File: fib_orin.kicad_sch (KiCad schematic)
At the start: 1 part, among them J1201 Orin Nano

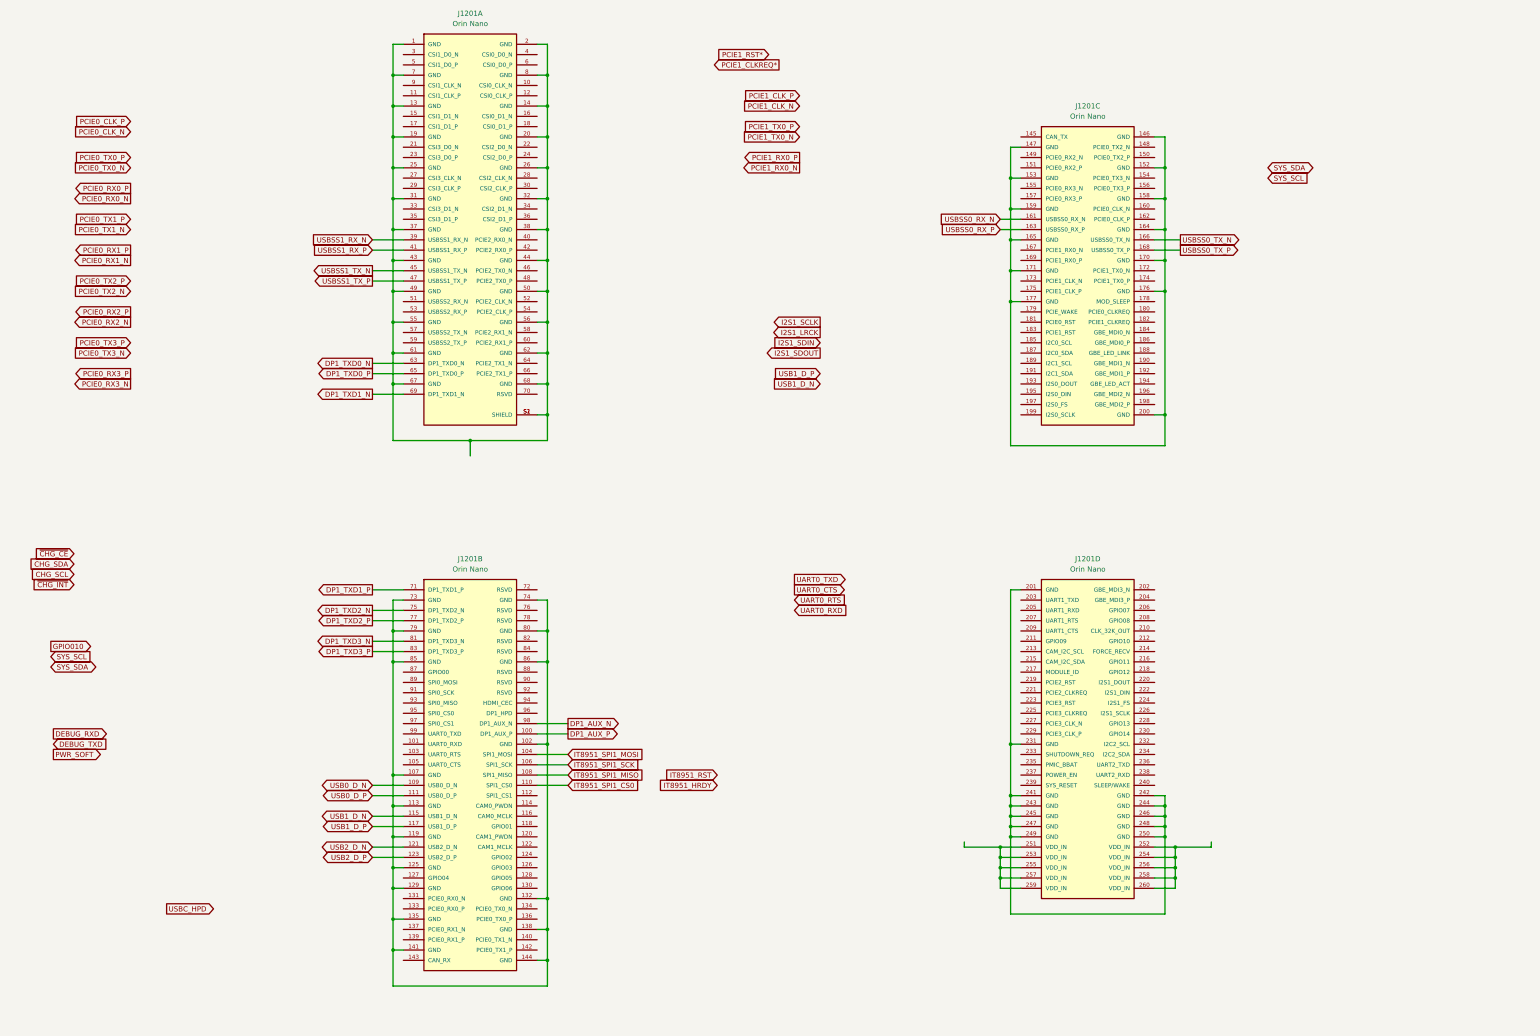
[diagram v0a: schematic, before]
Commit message: continuing schematic work for pcie and other high speed interfaces
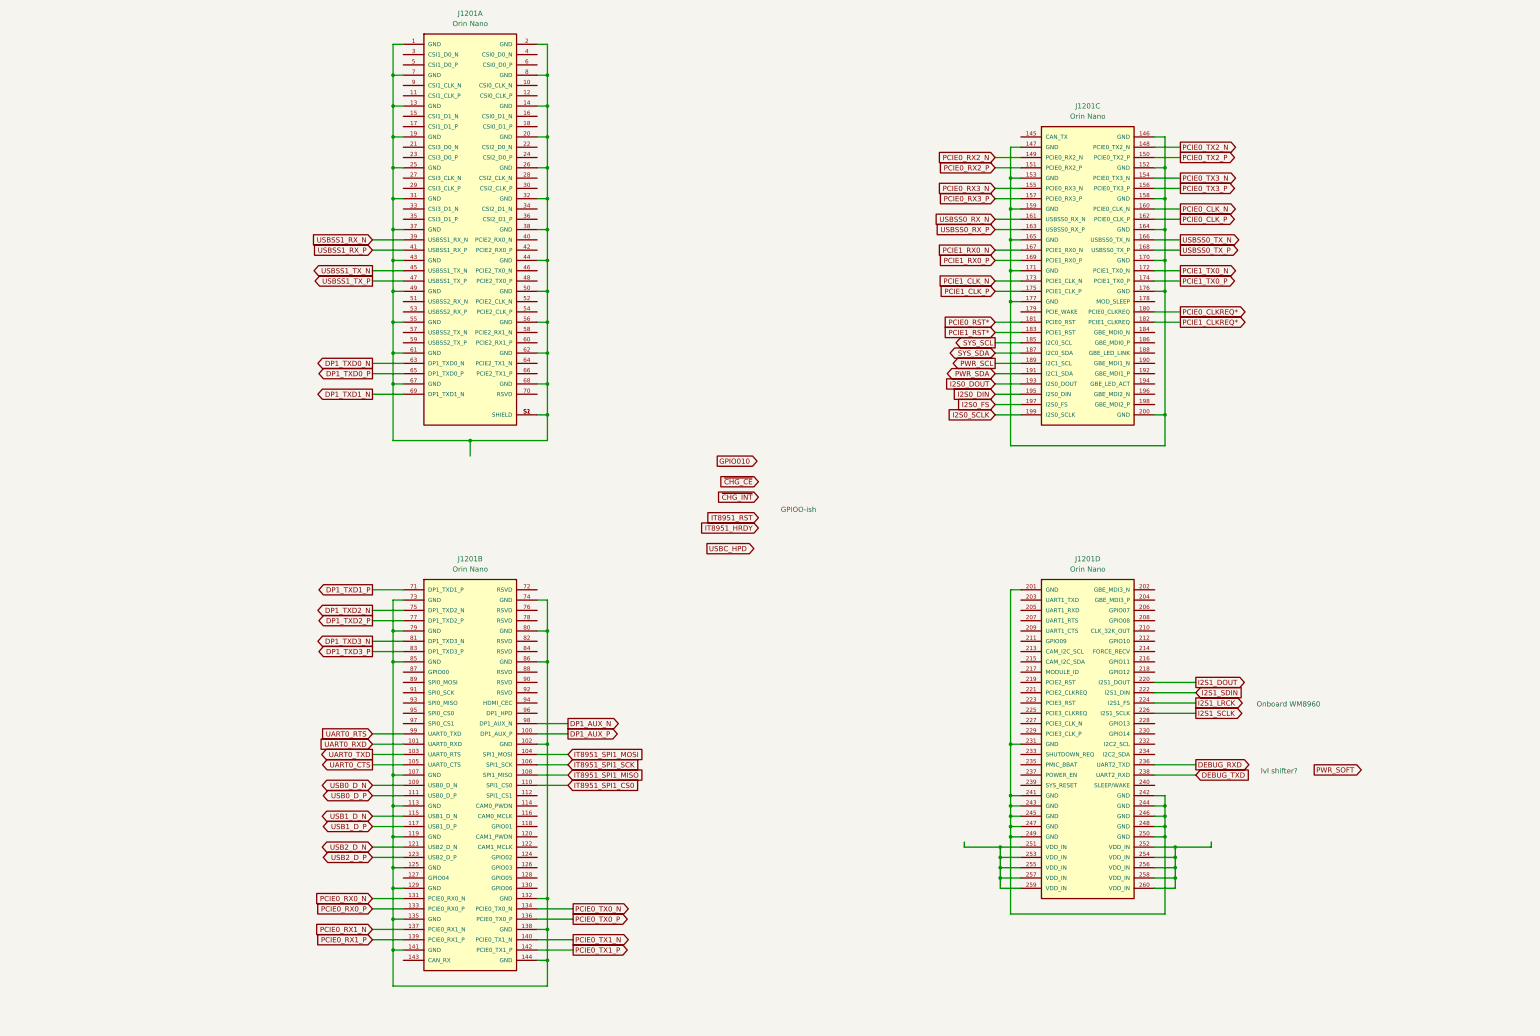
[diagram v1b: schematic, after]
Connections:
- net DEBUG_RXD: now also J1201.236 (UART2_TXD)
- net DEBUG_TXD: now also J1201.238 (UART2_RXD)
- net I2S1_LRCK: now also J1201.224 (I2S1_FS)
- net I2S1_SCLK: now also J1201.226 (I2S1_SCLK)
- net I2S1_SDIN: now also J1201.222 (I2S1_DIN)
- net PCIE0_CLK_N: now also J1201.160 (PCIE0_CLK_N)
- net PCIE0_CLK_P: now also J1201.162 (PCIE0_CLK_P)
- net PCIE0_RX0_N: now also J1201.131 (PCIE0_RX0_N)
- net PCIE0_RX0_P: now also J1201.133 (PCIE0_RX0_P)
- net PCIE0_RX1_N: now also J1201.137 (PCIE0_RX1_N)
- net PCIE0_RX1_P: now also J1201.139 (PCIE0_RX1_P)
- net PCIE0_RX2_N: now also J1201.149 (PCIE0_RX2_N)
- net PCIE0_RX2_P: now also J1201.151 (PCIE0_RX2_P)
- net PCIE0_RX3_N: now also J1201.155 (PCIE0_RX3_N)
- net PCIE0_RX3_P: now also J1201.157 (PCIE0_RX3_P)
- net PCIE0_TX0_N: now also J1201.134 (PCIE0_TX0_N)
- net PCIE0_TX0_P: now also J1201.136 (PCIE0_TX0_P)
- net PCIE0_TX1_N: now also J1201.140 (PCIE0_TX1_N)
- net PCIE0_TX1_P: now also J1201.142 (PCIE0_TX1_P)
- net PCIE0_TX2_N: now also J1201.148 (PCIE0_TX2_N)
- net PCIE0_TX2_P: now also J1201.150 (PCIE0_TX2_P)
- net PCIE0_TX3_N: now also J1201.154 (PCIE0_TX3_N)
- net PCIE0_TX3_P: now also J1201.156 (PCIE0_TX3_P)
- net PCIE1_CLKREQ*: now also J1201.182 (PCIE1_CLKREQ)
- net PCIE1_CLK_N: now also J1201.173 (PCIE1_CLK_N)
- net PCIE1_CLK_P: now also J1201.175 (PCIE1_CLK_P)
- net PCIE1_RST*: now also J1201.183 (PCIE1_RST)
- net PCIE1_RX0_N: now also J1201.167 (PCIE1_RX0_N)
- net PCIE1_RX0_P: now also J1201.169 (PCIE1_RX0_P)
- net PCIE1_TX0_N: now also J1201.172 (PCIE1_TX0_N)
- net PCIE1_TX0_P: now also J1201.174 (PCIE1_TX0_P)
- net SYS_SCL: now also J1201.185 (I2C0_SCL)
- net SYS_SDA: now also J1201.187 (I2C0_SDA)
- net UART0_CTS: now also J1201.105 (UART0_CTS)
- net UART0_RTS: now also J1201.99 (UART0_TXD)
- net UART0_RXD: now also J1201.101 (UART0_RXD)
- net UART0_TXD: now also J1201.103 (UART0_RTS)
- net I2S1_DOUT: now reaches J1201.220 (I2S1_DOUT)
- net PCIE0_CLKREQ*: now reaches J1201.180 (PCIE0_CLKREQ)
- net PCIE0_RST*: now reaches J1201.181 (PCIE0_RST)
- net PWR_SCL: now reaches J1201.189 (I2C1_SCL)
- net PWR_SDA: now reaches J1201.191 (I2C1_SDA)
- net I2S0_DOUT: now reaches J1201.193 (I2S0_DOUT)
- net I2S0_DIN: now reaches J1201.195 (I2S0_DIN)
- net I2S0_FS: now reaches J1201.197 (I2S0_FS)
- net I2S0_SCLK: now reaches J1201.199 (I2S0_SCLK)
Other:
- note added: "GPIOO-ish"
- note added: "Onboard WM8960"
- note added: "lvl shifter?"

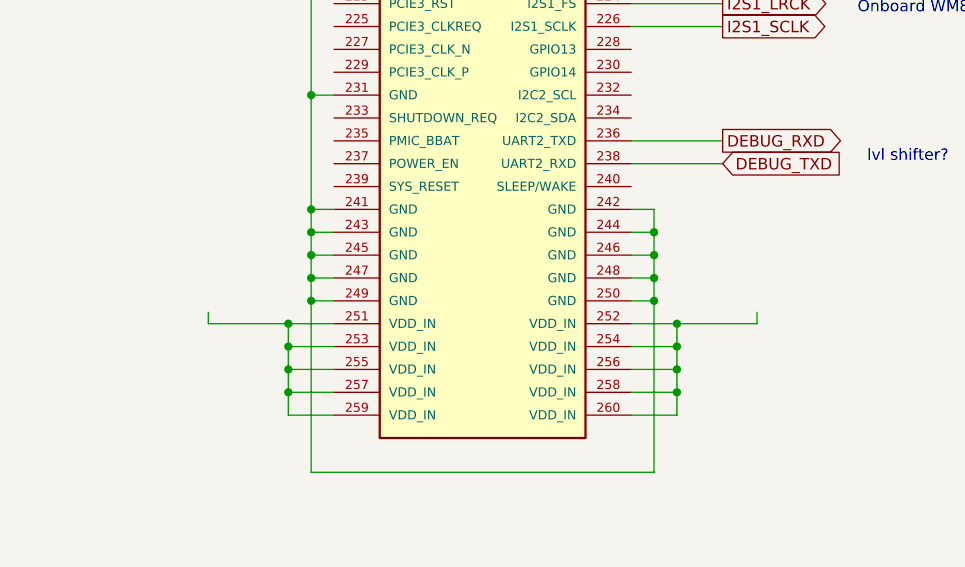
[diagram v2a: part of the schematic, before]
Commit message: added notest regarding the audio codec
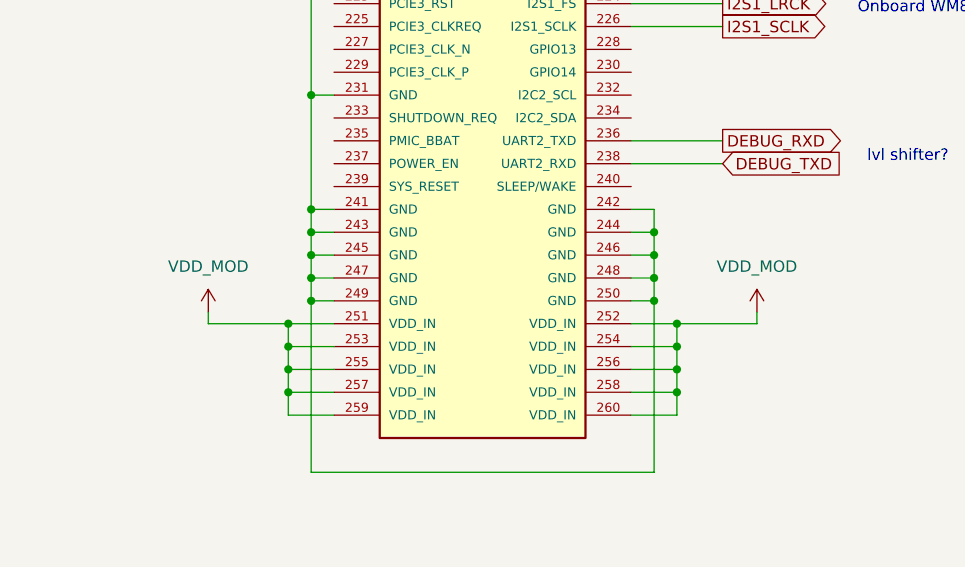
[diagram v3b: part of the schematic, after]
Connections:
- net VDD_MOD: now reaches J1201.251 (VDD_IN), J1201.253 (VDD_IN), J1201.255 (VDD_IN), J1201.257 (VDD_IN), J1201.259 (VDD_IN)
- net VDD_MOD: now also J1201.252 (VDD_IN), J1201.254 (VDD_IN), J1201.256 (VDD_IN), J1201.258 (VDD_IN), J1201.260 (VDD_IN)
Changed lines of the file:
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@@
+	)
+	(symbol
+		(lib_id "power:+5V")
+		(at 254 229.87 0)
+		(unit 1)
+		(exclude_from_sim no)
+		(in_bom yes)
+		(on_board yes)
+		(dnp no)
+		(fields_autoplaced yes)
+		(property "Reference" "#PWR01"
+			(at 254 233.68 0)
+			(effects
+				(font
+					(size 1.27 1.27)
+				)
+				(hide yes)
+			)
+		)
+		(property "Value" "VDD_MOD"
+			(at 254 224.79 0)
+			(effects
+				(font
+					(size 1.27 1.27)
+				)
+			)
+		)
+		(property "Footprint" ""
+			(at 254 229.87 0)
+			(effects
+				(font
+					(size 1.27 1.27)
+				)
+				(hide yes)
+			)
+		)
+		(property "Datasheet" ""
+			(at 254 229.87 0)
+			(effects
+				(font
+					(size 1.27 1.27)
+				)
+				(hide yes)
+			)
+		)
+		(property "Description" "Power symbol creates a global label with name \"+5V\""
+			(at 254 229.87 0)
+			(effects
+				(font
+					(size 1.27 1.27)
+				)
+				(hide yes)
+			)
+		)
+		(pin "1"
+		)
+		(instances
+			(project "Fibel2"
+				(path "/862c21e2-7ec9-4f80-a33c-aad02ea9423e/36a293ae-b0d7-4698-aa86-662a0ac946ae"
+					(reference "#PWR01")
+					(unit 1)
+				)
+			)
+		)
+	)
+	(symbol
+		(lib_id "power:+5V")
+		(at 314.96 229.87 0)
+		(unit 1)
+		(exclude_from_sim no)
+		(in_bom yes)
+		(on_board yes)
+		(dnp no)
+		(fields_autoplaced yes)
+		(property "Reference" "#PWR02"
+			(at 314.96 233.68 0)
+			(effects
+				(font
+					(size 1.27 1.27)
+				)
+				(hide yes)
+			)
+		)
+		(property "Value" "VDD_MOD"
+			(at 314.96 224.79 0)
+			(effects
+				(font
+					(size 1.27 1.27)
+				)
+			)
+		)
+		(property "Footprint" ""
+			(at 314.96 229.87 0)
+			(effects
+				(font
+					(size 1.27 1.27)
+				)
+				(hide yes)
+			)
+		)
+		(property "Datasheet" ""
+			(at 314.96 229.87 0)
+			(effects
+				(font
+					(size 1.27 1.27)
+				)
+				(hide yes)
+			)
+		)
+		(property "Description" "Power symbol creates a global label with name \"+5V\""
+			(at 314.96 229.87 0)
+			(effects
+				(font
+					(size 1.27 1.27)
+				)
+				(hide yes)
+			)
+		)
+		(pin "1"
+		)
+		(instances
+			(project "Fibel2"
+				(path "/862c21e2-7ec9-4f80-a33c-aad02ea9423e/36a293ae-b0d7-4698-aa86-662a0ac946ae"
+					(reference "#PWR02")
+					(unit 1)
+				)
+			)
+		)
 	)
 	(symbol

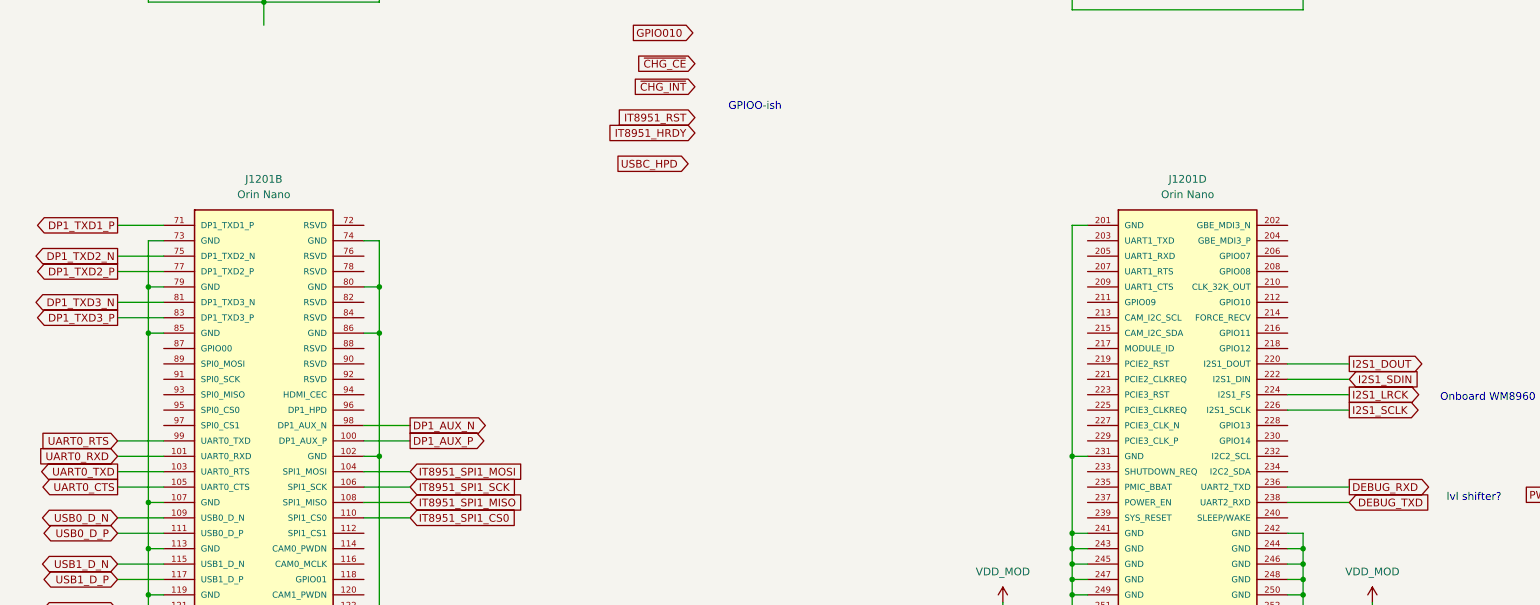
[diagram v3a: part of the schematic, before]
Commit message: added buck converter, refactoored peripherals and updated gpio/SPI/i2c mapping
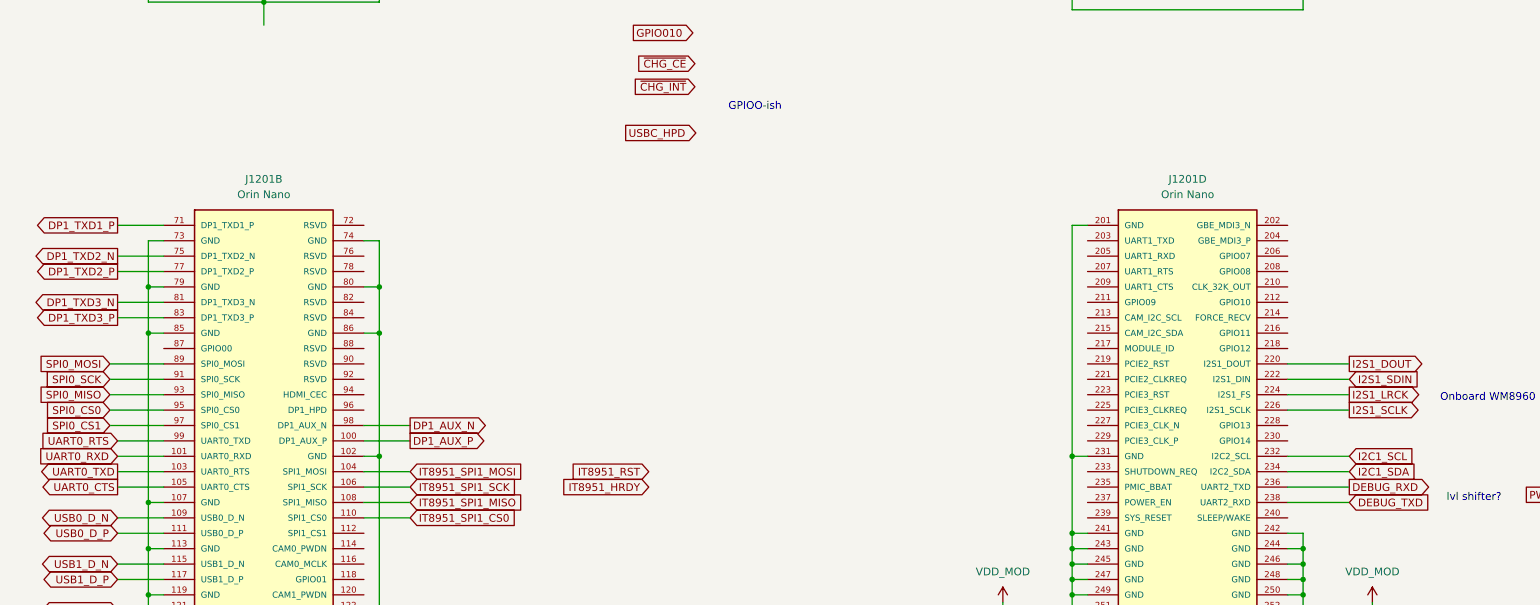
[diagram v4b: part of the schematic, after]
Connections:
- net SPI0_MOSI: now reaches J1201.89 (SPI0_MOSI)
- net SPI0_SCK: now reaches J1201.91 (SPI0_SCK)
- net SPI0_MISO: now reaches J1201.93 (SPI0_MISO)
- net SPI0_CS0: now reaches J1201.95 (SPI0_CS0)
- net SPI0_CS1: now reaches J1201.97 (SPI0_CS1)
- net I2C1_SCL: now reaches J1201.232 (I2C2_SCL)
- net I2C1_SDA: now reaches J1201.234 (I2C2_SDA)
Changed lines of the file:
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@@
 	(wire
 		(pts
+			(xy 106.68 195.58) (xy 115.57 195.58)
+		)
+		(stroke
+			(width 0)
+			(type default)
+		)
+	)
+	(wire
+		(pts
 			(xy 261.62 121.92) (xy 267.97 121.92)
 		)
@@
 	(wire
 		(pts
+			(xy 106.68 190.5) (xy 115.57 190.5)
+		)
+		(stroke
+			(width 0)
+			(type default)
+		)
+	)
+	(wire
+		(pts
 			(xy 311.15 195.58) (xy 300.99 195.58)
 		)
@@
 	(wire
 		(pts
+			(xy 311.15 208.28) (xy 300.99 208.28)
+		)
+		(stroke
+			(width 0)
+			(type default)
+		)
+	)
+	(wire
+		(pts
 			(xy 107.95 251.46) (xy 115.57 251.46)
 		)
@@
 	(wire
 		(pts
+			(xy 106.68 193.04) (xy 115.57 193.04)
+		)
+		(stroke
+			(width 0)
+			(type default)
+		)
+	)
+	(wire
+		(pts
 			(xy 303.53 223.52) (xy 303.53 220.98)
 		)
@@
 	(wire
 		(pts
+			(xy 311.15 205.74) (xy 300.99 205.74)
+		)
+		(stroke
+			(width 0)
+			(type default)
+		)
+	)
+	(wire
+		(pts
 			(xy 113.03 177.8) (xy 115.57 177.8)
 		)
@@
 	(wire
 		(pts
+			(xy 106.68 200.66) (xy 115.57 200.66)
+		)
+		(stroke
+			(width 0)
+			(type default)
+		)
+	)
+	(wire
+		(pts
 			(xy 113.03 55.88) (xy 113.03 63.5)
 		)
@@
 	(wire
 		(pts
+			(xy 106.68 198.12) (xy 115.57 198.12)
+		)
+		(stroke
+			(width 0)
+			(type default)
+		)
+	)
+	(wire
+		(pts
 			(xy 113.03 71.12) (xy 113.03 78.74)
 		)
@@
 		)
 	)
+	(global_label "I2C1_SDA"
+		(shape input)
+		(at 311.15 208.28 0)
+		(fields_autoplaced yes)
+		(effects
+			(font
+				(size 1.27 1.27)
+			)
+			(justify left)
+		)
+		(property "Intersheetrefs" "${INTERSHEET_REFS}"
+			(at 322.9647 208.28 0)
+			(effects
+				(font
+					(size 1.27 1.27)
+				)
+				(justify left)
+				(hide yes)
+			)
+		)
+	)
 	(global_label "USB2_D_P"
 		(shape bidirectional)
@@
 	(global_label "IT8951_RST"
 		(shape input)
-		(at 203.2 149.86 180)
+		(at 195.58 208.28 180)
+		(fields_autoplaced yes)
+		(effects
+			(font
+				(size 1.27 1.27)
+			)
+			(justify right)
+		)
+		(property "Intersheetrefs" "${INTERSHEET_REFS}"
+			(at 181.7697 208.28 0)
+			(effects
+				(font
+					(size 1.27 1.27)
+				)
+				(justify right)
+				(hide yes)
+			)
+		)
+	)
+	(global_label "SPI0_MISO"
+		(shape input)
+		(at 106.68 195.58 180)
 		(fields_autoplaced yes)
 		(effects
@@
 		)
 		(property "Intersheetrefs" "${INTERSHEET_REFS}"
-			(at 189.3897 149.86 0)
+			(at 93.8372 195.58 0)
 			(effects
 				(font
@@
 		)
 	)
+	(global_label "SPI0_SCK"
+		(shape input)
+		(at 106.68 193.04 180)
+		(fields_autoplaced yes)
+		(effects
+			(font
+				(size 1.27 1.27)
+			)
+			(justify right)
+		)
+		(property "Intersheetrefs" "${INTERSHEET_REFS}"
+			(at 94.6839 193.04 0)
+			(effects
+				(font
+					(size 1.27 1.27)
+				)
+				(justify right)
+				(hide yes)
+			)
+		)
+	)
 	(global_label "USBSS0_RX_N"
 		(shape input)
@@
 		)
 	)
+	(global_label "SPI0_CS0"
+		(shape input)
+		(at 106.68 198.12 180)
+		(fields_autoplaced yes)
+		(effects
+			(font
+				(size 1.27 1.27)
+			)
+			(justify right)
+		)
+		(property "Intersheetrefs" "${INTERSHEET_REFS}"
+			(at 94.7444 198.12 0)
+			(effects
+				(font
+					(size 1.27 1.27)
+				)
+				(justify right)
+				(hide yes)
+			)
+		)
+	)
 	(global_label "PCIE0_RST*"
 		(shape input)
@@
 		)
 	)
+	(global_label "SPI0_MOSI"
+		(shape input)
+		(at 106.68 190.5 180)
+		(fields_autoplaced yes)
+		(effects
+			(font
+				(size 1.27 1.27)
+			)
+			(justify right)
+		)
+		(property "Intersheetrefs" "${INTERSHEET_REFS}"
+			(at 93.8372 190.5 0)
+			(effects
+				(font
+					(size 1.27 1.27)
+				)
+				(justify right)
+				(hide yes)
+			)
+		)
+	)
 	(global_label "USB1_D_N"
 		(shape bidirectional)
@@
 	(global_label "IT8951_HRDY"
 		(shape input)
-		(at 203.2 152.4 180)
+		(at 195.58 210.82 180)
 		(fields_autoplaced yes)
 		(effects
@@
 		)
 		(property "Intersheetrefs" "${INTERSHEET_REFS}"
-			(at 187.8777 152.4 0)
+			(at 180.2577 210.82 0)
 			(effects
 				(font
@@
 		)
 	)
+	(global_label "SPI0_CS1"
+		(shape input)
+		(at 106.68 200.66 180)
+		(fields_autoplaced yes)
+		(effects
+			(font
+				(size 1.27 1.27)
+			)
+			(justify right)
+		)
+		(property "Intersheetrefs" "${INTERSHEET_REFS}"
+			(at 94.7444 200.66 0)
+			(effects
+				(font
+					(size 1.27 1.27)
+				)
+				(justify right)
+				(hide yes)
+			)
+		)
+	)
 	(global_label "PCIE0_RX0_P"
 		(shape input)
@@
 	(global_label "USBC_HPD"
 		(shape output)
-		(at 190.5 157.48 0)
+		(at 191.77 152.4 0)
 		(effects
 			(font
@@
 		)
 		(property "Intersheetrefs" "${INTERSHEET_REFS}"
-			(at 206.375 157.48 0)
+			(at 207.645 152.4 0)
 			(effects
 				(font
@@
 				(hide yes)
 			)
+		)
+	)
+	(global_label "I2C1_SCL"
+		(shape input)
+		(at 311.15 205.74 0)
+		(fields_autoplaced yes)
+		(effects
+			(font
+				(size 1.27 1.27)
+			)
+			(justify left)
+		)
+		(property "Intersheetrefs" "${INTERSHEET_REFS}"
+			(at 322.9042 205.74 0)
+			(effects
+				(font
+					(size 1.27 1.27)
+				)
+				(justify left)
+				(hide yes)
+			)
